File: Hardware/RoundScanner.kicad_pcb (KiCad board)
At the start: 2 copper layers, 49.1 x 49.1 mm, 71 parts, among them J1 I2C Debug, J2 I2C, J3 I2C, Q1 BSS138DW-7-F, U1 OPA2376xxD, U2 NAU7802SGI, U3 LM285D-2.5, U5 TLC59208FIPWR, U6 AS7341-DLGT, U7 AP7312-1833W6-7

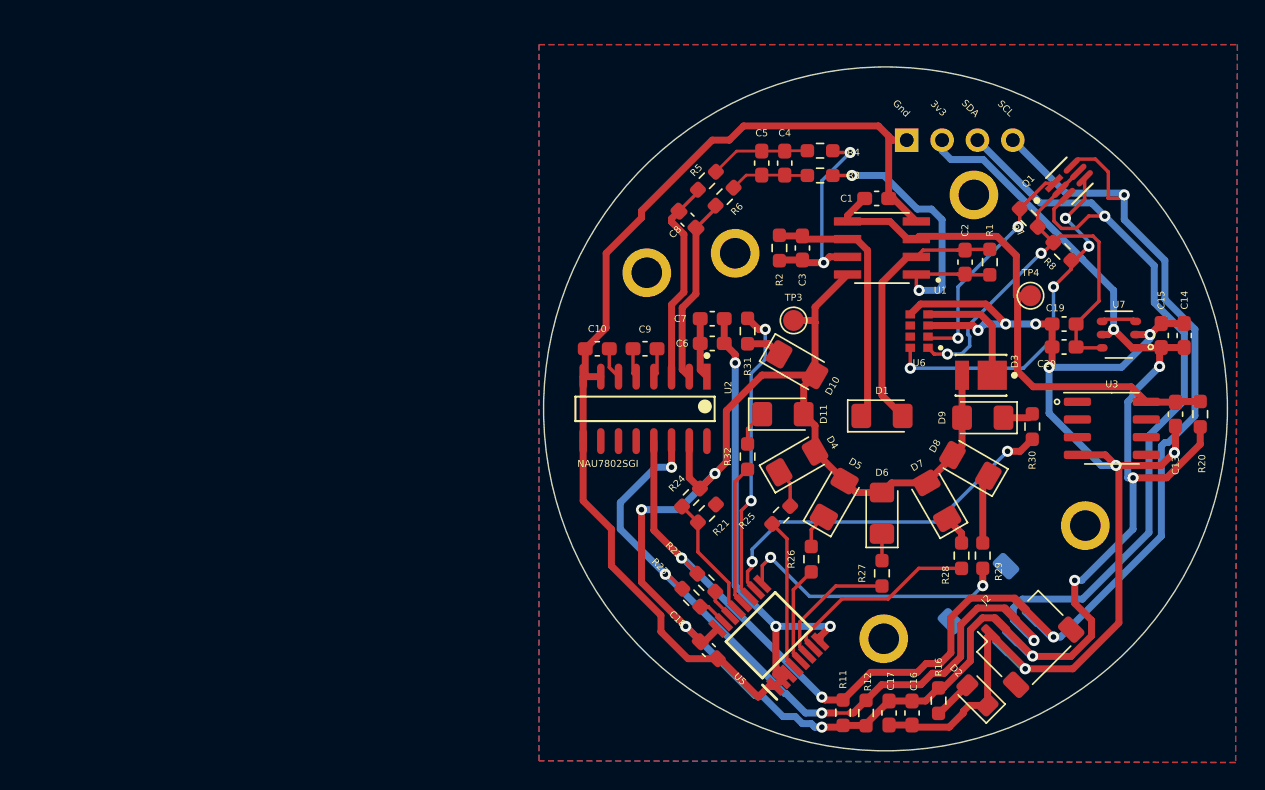
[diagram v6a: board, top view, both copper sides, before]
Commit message: initial branch commit with rought layout changes
Signed-off-by: Lawrence Kincheloe <lawrence.kincheloe@mavericktechok.com>
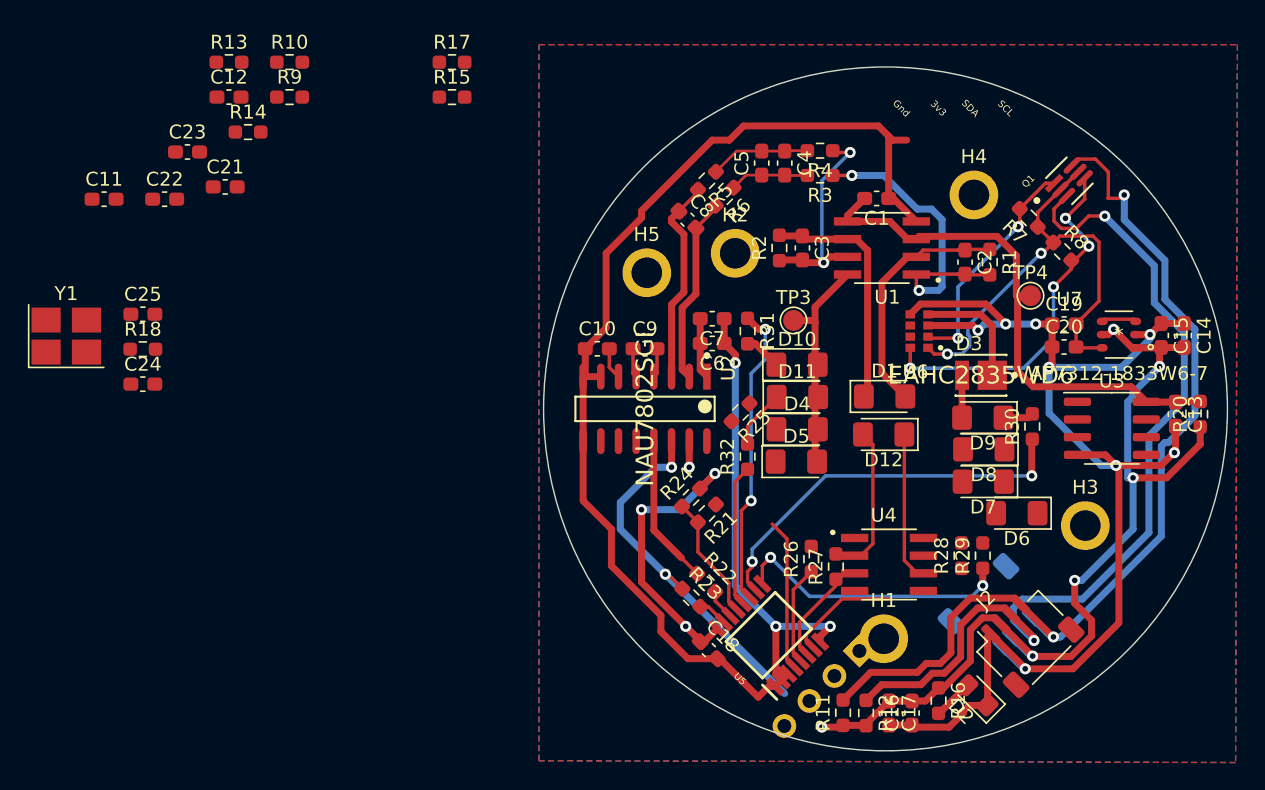
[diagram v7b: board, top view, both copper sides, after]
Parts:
- added C11: 100n, Capacitor_SMD:C_0603_1608Metric_Pad1.08x0.95mm_HandSolder, F.Cu at (33.4, 92.0)
- added C12: 51p, Capacitor_SMD:C_0603_1608Metric_Pad1.08x0.95mm_HandSolder, F.Cu at (42.4, 84.7)
- added C21: 51p, Capacitor_SMD:C_0603_1608Metric_Pad1.08x0.95mm_HandSolder, F.Cu at (42.1, 91.1)
- added C22: 47n, Capacitor_SMD:C_0603_1608Metric_Pad1.08x0.95mm_HandSolder, F.Cu at (37.8, 92.0)
- added C23: 100p, Capacitor_SMD:C_0603_1608Metric_Pad1.08x0.95mm_HandSolder, F.Cu at (39.4, 88.6)
- added C24: 18pF, Capacitor_SMD:C_0603_1608Metric_Pad1.08x0.95mm_HandSolder, F.Cu at (36.2, 105.3)
- added C25: 18pF, Capacitor_SMD:C_0603_1608Metric_Pad1.08x0.95mm_HandSolder, F.Cu at (36.2, 100.3)
- added D12: 0090-3111-185, Diode_SMD:D_1206_3216Metric_Pad1.42x1.75mm_HandSolder, F.Cu at (89.4, 108.9)
- added R10: 240k, Resistor_SMD:R_0603_1608Metric_Pad0.98x0.95mm_HandSolder, F.Cu at (46.7, 82.2)
- added R13: 301, Resistor_SMD:R_0603_1608Metric_Pad0.98x0.95mm_HandSolder, F.Cu at (42.4, 82.2)
- added R14: 301, Resistor_SMD:R_0603_1608Metric_Pad0.98x0.95mm_HandSolder, F.Cu at (43.8, 87.2)
- added R15: 51, Resistor_SMD:R_0603_1608Metric_Pad0.98x0.95mm_HandSolder, F.Cu at (58.4, 84.7)
- added R17: 51, Resistor_SMD:R_0603_1608Metric_Pad0.98x0.95mm_HandSolder, F.Cu at (58.4, 82.2)
- added R18: 270, Resistor_SMD:R_0603_1608Metric_Pad0.98x0.95mm_HandSolder, F.Cu at (36.2, 102.8)
- added R9: 240k, Resistor_SMD:R_0603_1608Metric_Pad0.98x0.95mm_HandSolder, F.Cu at (46.7, 84.7)
- added U4: OPA2376xxD, OPA2376AID:SOIC127P599X175-8N, F.Cu at (89.8, 118.2)
- added Y1: Crystal_GND23, Crystal:Crystal_SMD_3225-4Pin_3.2x2.5mm_HandSoldering, F.Cu at (30.7, 101.8)
- C1, C10, C13, C14, C15, C16, C17, C18, C19, C2, C20, C3, C4, C5, C6, C7, C8: footprint PlasticScannerLibrary:C_0603_1608Metric_Pad1.08x0.95mm_HandSolder -> Capacitor_SMD:C_0603_1608Metric_Pad1.08x0.95mm_HandSolder
- C9: value 470pF -> 0.1uF; footprint PlasticScannerLibrary:C_0603_1608Metric_Pad1.08x0.95mm_HandSolder -> Capacitor_SMD:C_0603_1608Metric_Pad1.08x0.95mm_HandSolder
- D1: footprint PlasticScannerLibrary:D_1206_3216Metric_Pad1.42x1.75mm_HandSolder -> Diode_SMD:D_1206_3216Metric_Pad1.42x1.75mm_HandSolder
- D10, D11, D4, D5, D6, D7, D8, D9: footprint PlasticScannerLibrary:LED_1206_3216Metric_Pad1.42x1.75mm_HandSolder -> LED_SMD:LED_1206_3216Metric_Pad1.42x1.75mm_HandSolder
- D2: footprint PlasticScannerLibrary:LED_0805_2012Metric_Pad1.15x1.40mm_HandSolder -> LED_SMD:LED_0805_2012Metric_Pad1.15x1.40mm_HandSolder
- D3: footprint PlasticScannerLibrary:Everlight-EAHC2835WD6-MFG -> Everlight-EAHC2835WD6:Everlight-EAHC2835WD6-MFG
- H1, H2, H3, H4, H5: footprint PlasticScannerLibrary:MountingHole_2.2mm_M2_ISO7380_Pad -> MountingHole:MountingHole_2.2mm_M2_ISO7380_Pad
- J1: footprint PlasticScannerLibrary:PinHeader_1x04_P2.54mm_Vertical -> Connector_PinHeader_2.54mm:PinHeader_1x04_P2.54mm_Vertical
- J2, J3: footprint PlasticScannerLibrary:JST_SH_SM04B-SRSS-TB_1x04-1MP_P1.00mm_Horizontal -> Connector_JST:JST_SH_SM04B-SRSS-TB_1x04-1MP_P1.00mm_Horizontal
- R1, R11, R12, R16, R2, R20, R21, R22, R23, R24, R25, R26, R27, R28, R29, R3, R30, R31, R32, R4, R5, R6, R7, R8: footprint PlasticScannerLibrary:R_0603_1608Metric_Pad0.98x0.95mm_HandSolder -> Resistor_SMD:R_0603_1608Metric_Pad0.98x0.95mm_HandSolder
- TP3, TP4: footprint PlasticScannerLibrary:TestPoint_Pad_D1.5mm -> TestPoint:TestPoint_Pad_D1.5mm
- U1: footprint PlasticScannerLibrary:SOIC127P599X175-8N -> OPA2376AID:SOIC127P599X175-8N
- U2: footprint PlasticScannerLibrary:Nuvoton-NAU7802SGI -> Nuvoton-NAU7802SGI:Nuvoton-NAU7802SGI
- U3: footprint PlasticScannerLibrary:SOIC-8_3.9x4.9mm_P1.27mm -> Package_SO:SOIC-8_3.9x4.9mm_P1.27mm
- U6: footprint PlasticScannerLibrary:PSON80P310X200X110-8N -> AS7341-DLGT:PSON80P310X200X110-8N
- U7: footprint PlasticScannerLibrary:AP7312-1833W6-7 -> AP7312-1833W6-7:AP7312-1833W6-7
- moved J1 36.8 mm to (87.7, 124.4), turned to 135 degrees
- moved D6 9.69 mm to (99.0, 114.6), turned to 180 degrees
- moved R25 7.92 mm to (79.1, 107.3), turned to -135 degrees
- moved D5 3.82 mm to (83.1, 110.8), turned to 0 degrees
- moved D7 3.61 mm to (96.6, 112.3), turned to 180 degrees
- moved R27 3.35 mm to (86.0, 118.4)
- moved D4 2.34 mm to (83.2, 108.5), turned to 0 degrees
- moved D11 1.61 mm to (83.2, 106.2)
- moved D8 1.50 mm to (96.6, 110.0), turned to 180 degrees
- moved D1 1.41 mm to (89.5, 106.2)
- turned D10 to 0 degrees
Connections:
- H1 pad 1: (no net) -> GND
- H2 pad 1: (no net) -> GND
- H3 pad 1: (no net) -> GND
- H4 pad 1: (no net) -> GND
- H5 pad 1: (no net) -> GND
- U2 pad 10: unconnected-(U2-Pad10) -> Net-(U2-Pad10)
- U2 pad 11: unconnected-(U2-Pad11) -> Net-(U2-Pad11)
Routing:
- net +3V3: track 171.4 -> 108.6 mm, vias 9 -> 10
- net SCL: track 104.1 -> 78.6 mm, vias 4 -> 2
- net SDA: track 126.5 -> 108.3 mm, vias 5 -> 4
- net Net-(C21-Pad1): track 0.00 -> 10.8 mm
- net Net-(C12-Pad1): track 0.00 -> 9.80 mm
- net Net-(R28-Pad1): track 14.3 -> 8.15 mm
- net Net-(D8-Pad1): track 5.40 -> 0.00 mm
- net Net-(R27-Pad1): track 9.54 -> 6.22 mm
- net Net-(D4-Pad1): track 2.75 -> 0.00 mm
- net Net-(D5-Pad1): track 2.49 -> 0.00 mm
- net Net-(D7-Pad1): track 2.16 -> 0.00 mm
- net Net-(D6-Pad1): track 1.92 -> 0.00 mm
- net Net-(D11-Pad1): track 2.57 -> 4.24 mm
- net Net-(R30-Pad1): track 26.7 -> 28.2 mm
- net Net-(C3-Pad1): track 18.9 -> 17.4 mm
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- added copper zone on In2.Cu, net +3V3
- added copper zone on In1.Cu, net GND
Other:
- copper layers 2 -> 4

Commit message: added -backups to gitignore lots of layout changes.
Signed-off-by: lokimetasmith <lokimail@gmail.com>
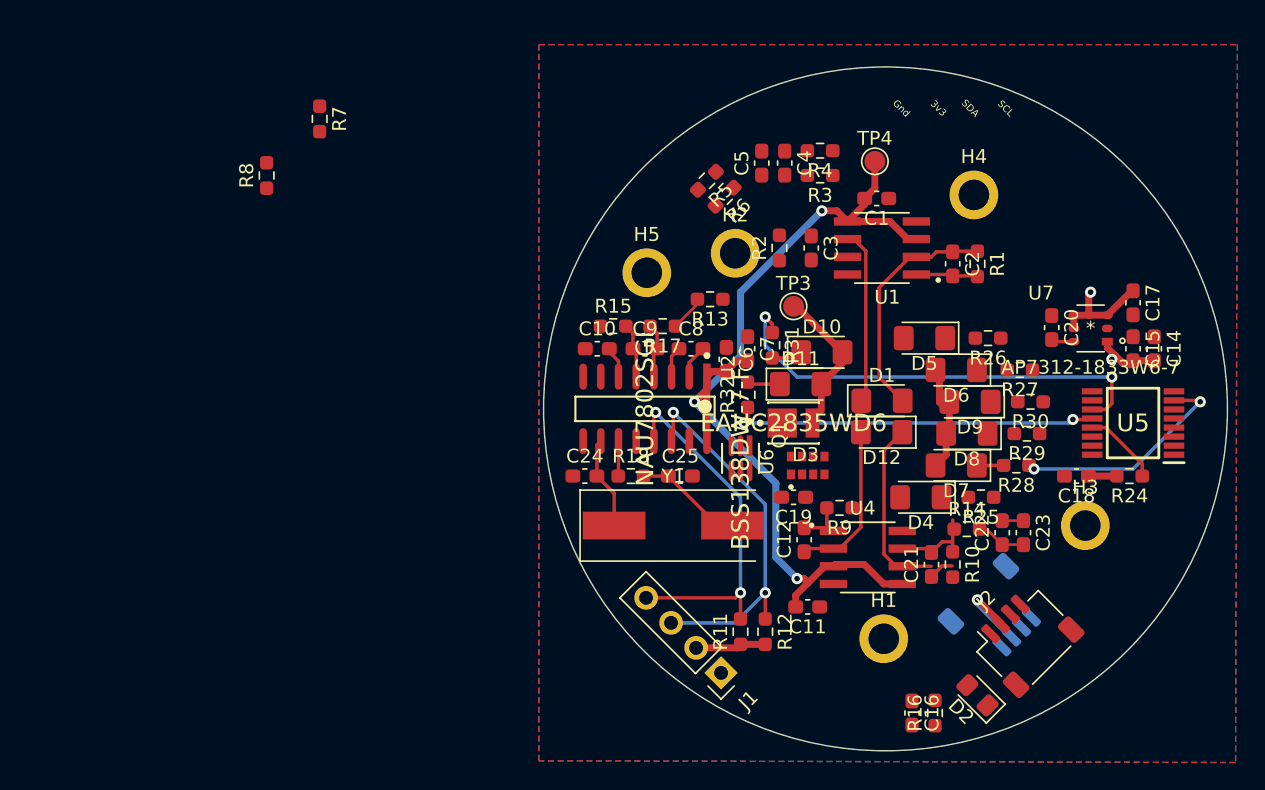
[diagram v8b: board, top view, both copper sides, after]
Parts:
- removed C13: 100n, Capacitor_SMD:C_0603_1608Metric_Pad1.08x0.95mm_HandSolder
- removed R20: 435, Resistor_SMD:R_0603_1608Metric_Pad0.98x0.95mm_HandSolder
- removed R21, R22, R23: 0, Resistor_SMD:R_0603_1608Metric_Pad0.98x0.95mm_HandSolder
- removed U3: LM285D-2.5, Package_SO:SOIC-8_3.9x4.9mm_P1.27mm
- J1: footprint Connector_PinHeader_2.54mm:PinHeader_1x04_P2.54mm_Vertical -> Connector_PinSocket_2.54mm:PinSocket_1x04_P2.54mm_Vertical; moved to F.Cu
- Q1: footprint PlasticScannerLibrary:Diodes_Inc._-_BSS138DW-7-F-A -> BSS138DW-7-F-A:Diodes_Inc._-_BSS138DW-7-F-A
- U5: footprint PlasticScannerLibrary:SOP65P640X120-16N -> TLC59208FIPWR:SOP65P640X120-16N
- Y1: footprint Crystal:Crystal_SMD_3225-4Pin_3.2x2.5mm_HandSoldering -> Crystal:Crystal_SMD_HC49-SD
- moved C23 66.0 mm to (99.4, 116.0), turned to -90 degrees
- moved C22 64.7 mm to (97.9, 116.0), turned to 90 degrees
- moved R10 59.8 mm to (94.4, 118.2), turned to -90 degrees
- moved R14 59.0 mm to (95.4, 115.7)
- moved C11 58.4 mm to (83.9, 121.3), turned to 180 degrees
- moved C21 57.5 mm to (92.8, 118.2), turned to 90 degrees
- moved R8 57.4 mm to (45.1, 90.3), turned to 90 degrees
- moved C12 52.1 mm to (83.7, 116.5), turned to 90 degrees
- moved R7 51.4 mm to (48.9, 86.2), turned to -90 degrees
- moved R9 49.3 mm to (86.2, 114.2), turned to 180 degrees
- moved Y1 45.7 mm to (74.3, 115.4)
- moved C25 40.3 mm to (74.8, 111.9)
- moved R13 38.5 mm to (76.9, 99.2), turned to 180 degrees
- moved R18 36.2 mm to (71.2, 111.9)
- moved C17 34.3 mm to (107.3, 99.4)
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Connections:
- C6 pad 2: Net-(C6-Pad2) -> +2V5
- C7 pad 2: Net-(C6-Pad2) -> +2V5
- R24 pad 1: Net-(R21-Pad2) -> /LED/LED RESET
- U2 pad 1: Net-(C6-Pad2) -> +2V5
- U2 pad 16: unconnected-(U2-Pad16) -> +2V5
- U5 pad 13: Net-(R21-Pad2) -> /LED/LED RESET
- U5 pad 14: Net-(R22-Pad2) -> SCL
- U5 pad 15: Net-(R23-Pad2) -> SDA
- U7 pad 3: Net-(U7-Pad3) -> +3V3
- U7 pad 4: Net-(U7-Pad3) -> +3V3
- Y1 pad 2: GND -> Net-(C25-Pad1)
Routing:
- net GND: track 200.1 -> 0.00 mm, vias 11 -> 0
- net SDA: track 108.3 -> 27.2 mm, vias 4 -> 2
- net +3V3: track 108.6 -> 42.2 mm, vias 10 -> 3
- net SCL: track 78.6 -> 26.4 mm
- net +1V8: track 34.0 -> 1.44 mm, vias 2 -> 0
- net Net-(R30-Pad1): track 28.2 -> 0.00 mm, vias 2 -> 0
- net /MCU + IO/SDA_2v: track 26.6 -> 0.00 mm, vias 4 -> 0
- net +2V5: track 38.9 -> 64.9 mm, vias 0 -> 3
- net Net-(R29-Pad1): track 20.1 -> 0.00 mm, vias 2 -> 0
- net Net-(C2-Pad2): track 21.8 -> 4.24 mm, vias 2 -> 0
- net /MCU + IO/SCL_2v: track 16.6 -> 0.00 mm, vias 2 -> 0
- net Net-(R32-Pad1): track 10.2 -> 26.3 mm, vias 0 -> 2
- net Net-(C3-Pad2): track 15.3 -> 0.00 mm, vias 2 -> 0
- net Net-(C8-Pad1): track 14.9 -> 2.22 mm
- net Net-(C8-Pad2): track 13.5 -> 2.41 mm
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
